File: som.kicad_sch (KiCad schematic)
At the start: 31 parts, among them J14 Conn_01x04, M1 jetson-orin-nx/nano-module, Q1 PJE138K, U4 NTS0102GT

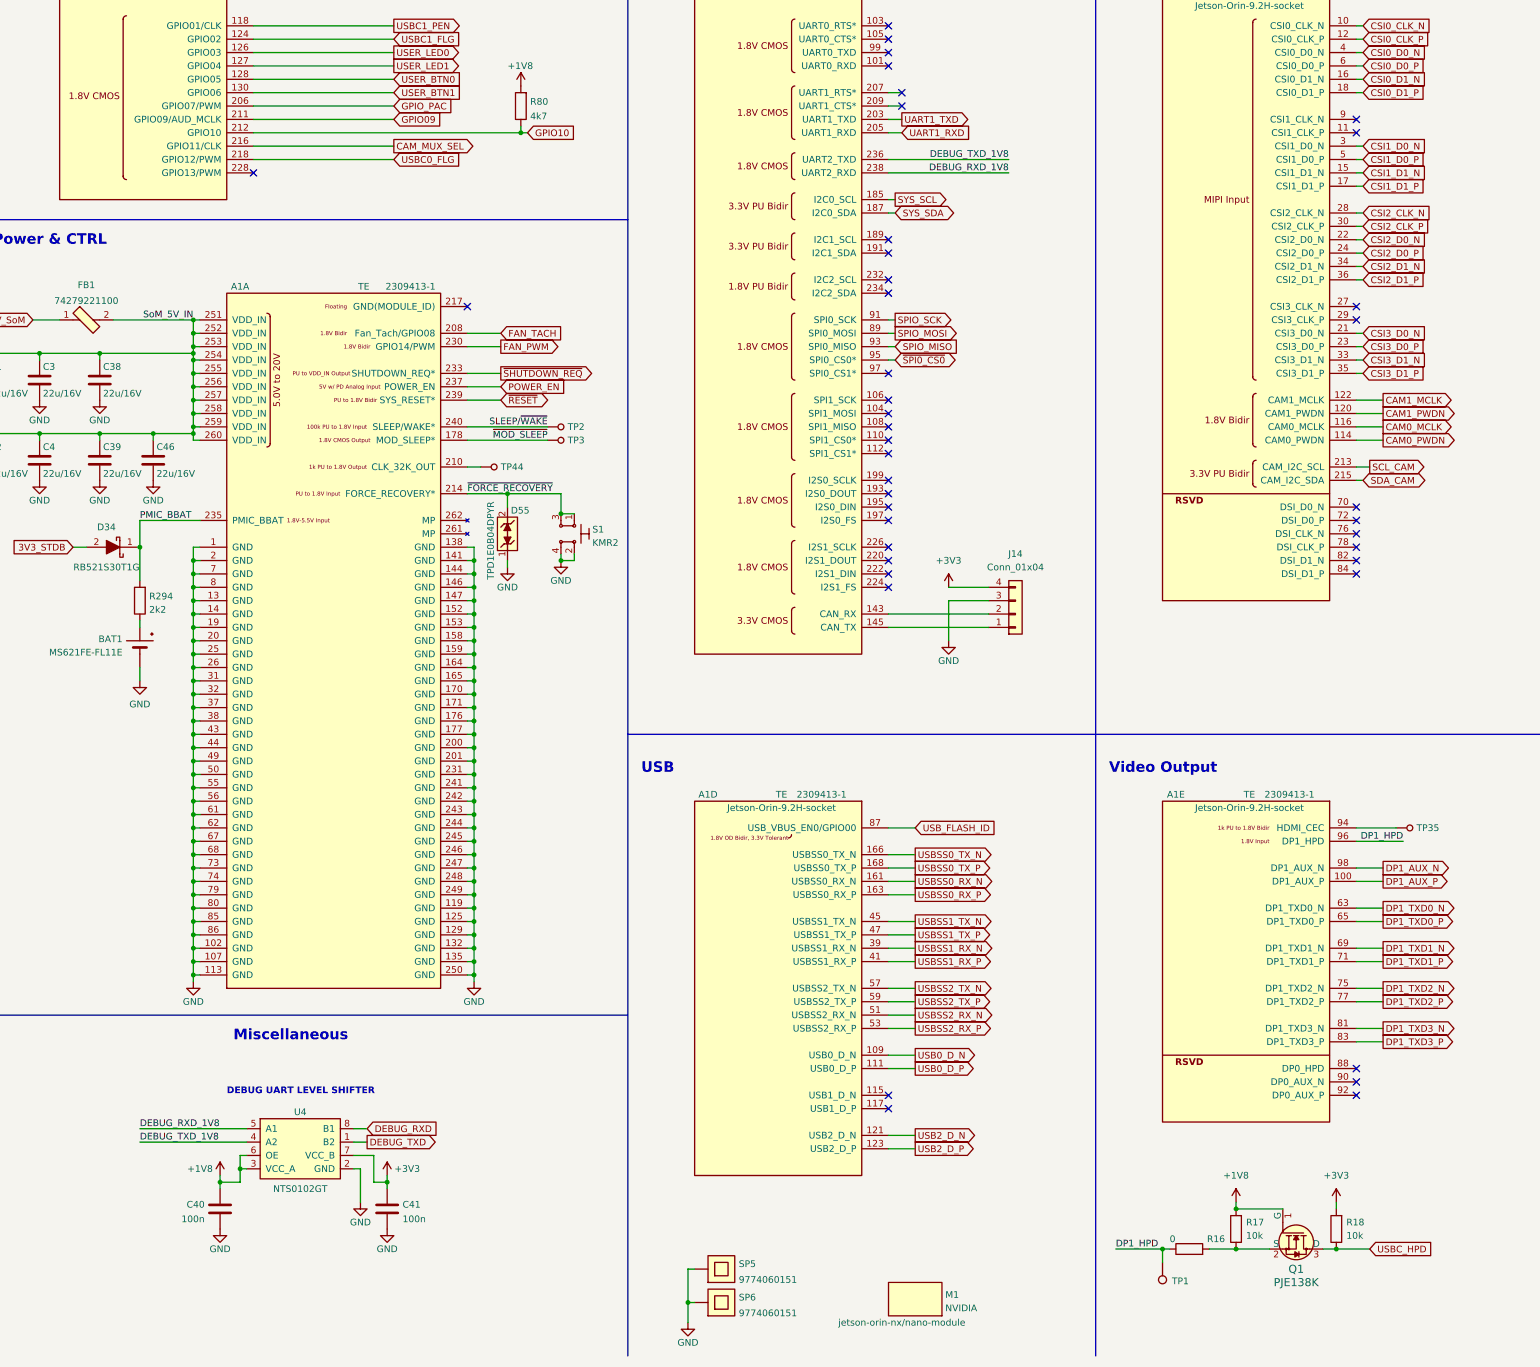
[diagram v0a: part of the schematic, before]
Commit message: Schematic V1 and footprints assigned
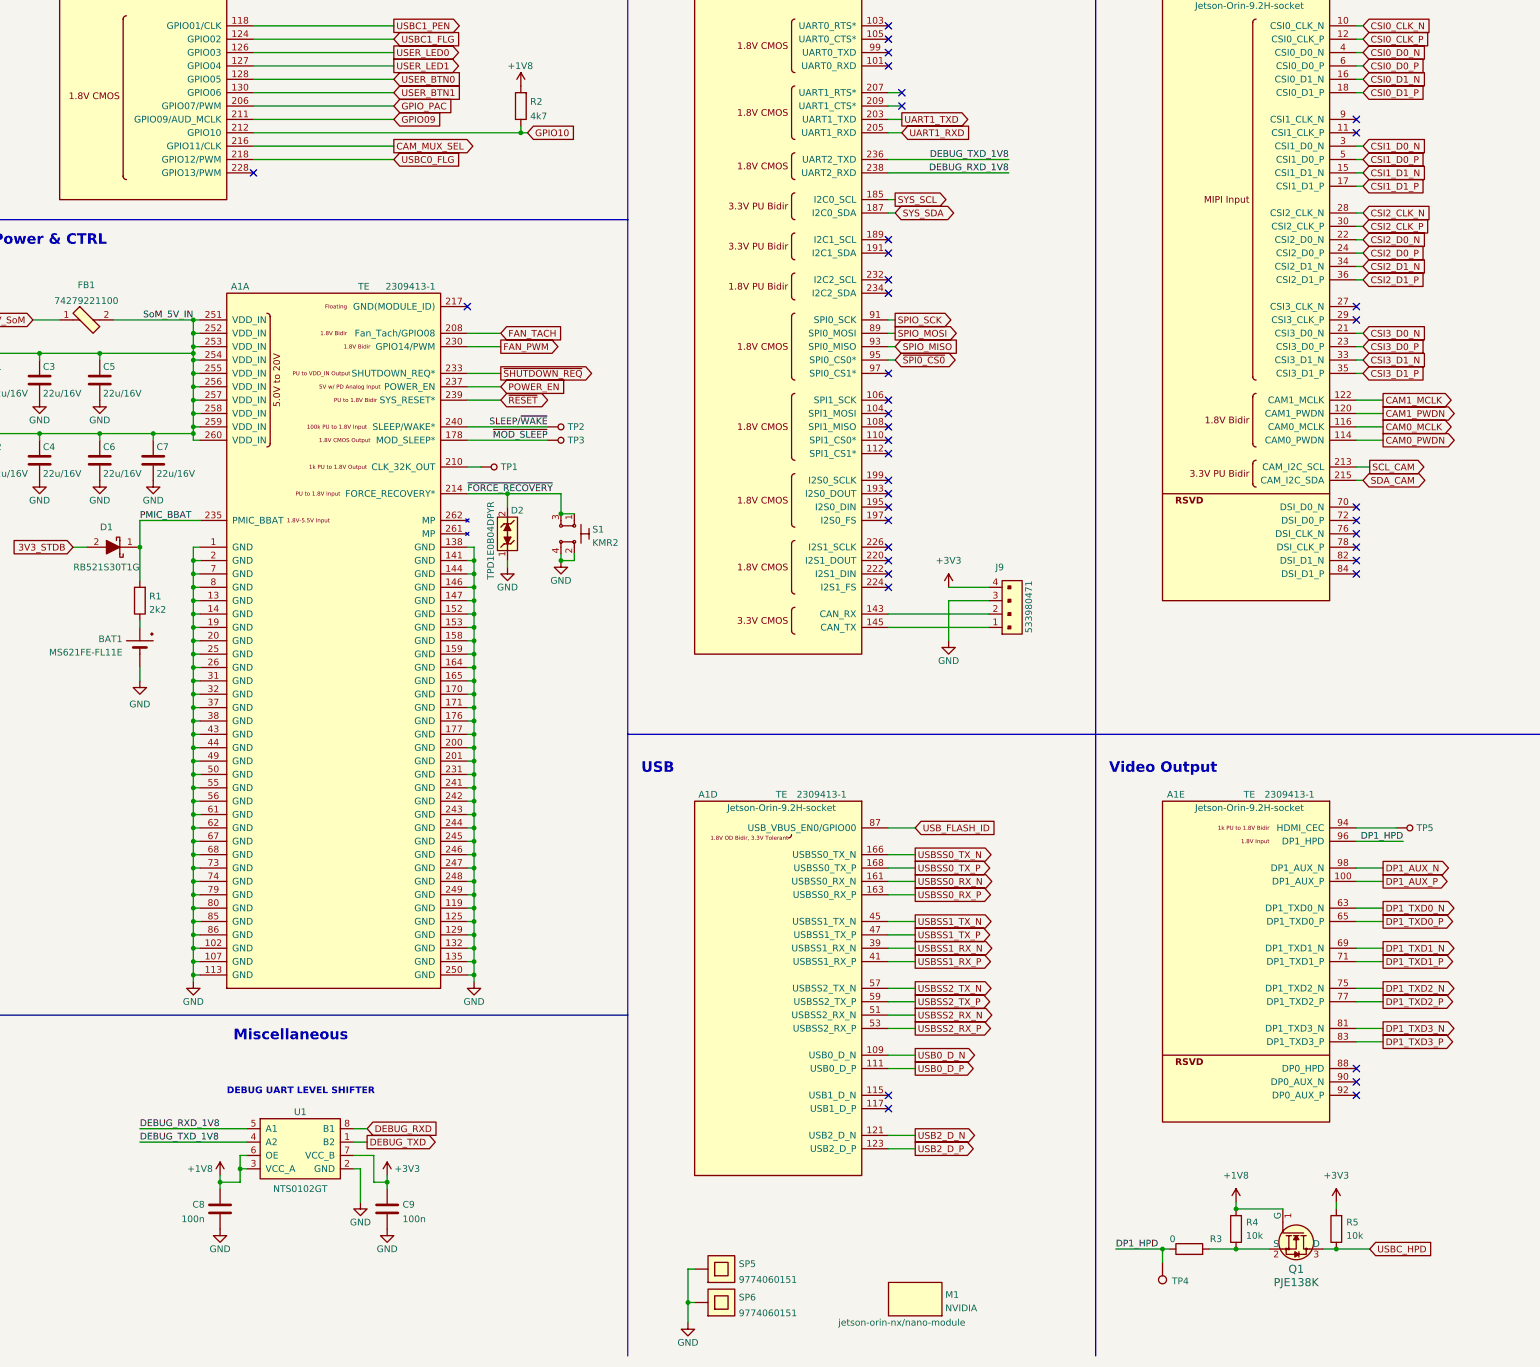
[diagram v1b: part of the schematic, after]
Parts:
- removed J14: Conn_01x04, symbol Connector_Generic:Conn_01x04
- added J9: 533980471, jetson-orin-baseboard-footprints:Molex_PicoBlade_53398-0471_1x04-1MP_P1.25mm_Vertical, symbol jetson-orin-baseboard:533980471
- R3: renamed from R16; footprint (none) -> jetson-orin-baseboard-footprints:0402-res
- R4: renamed from R17; footprint (none) -> jetson-orin-baseboard-footprints:0402-res
- R5: renamed from R18; footprint (none) -> jetson-orin-baseboard-footprints:0402-res
- TP4: renamed from TP1; footprint (none) -> jetson-orin-baseboard-footprints:Testpoint_smd_0_75mm
- renumbered C38 to C5, C39 to C6, C46 to C7, C40 to C8, C41 to C9, D34 to D1, D55 to D2, R294 to R1, R80 to R2, TP44 to TP1, TP35 to TP5, U4 to U1
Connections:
- net +3V3: now also J9.4
- net GND: now also J9.3
- net at A1.143 (CAN_RX): now also J9.2
- net at A1.145 (CAN_TX): now also J9.1

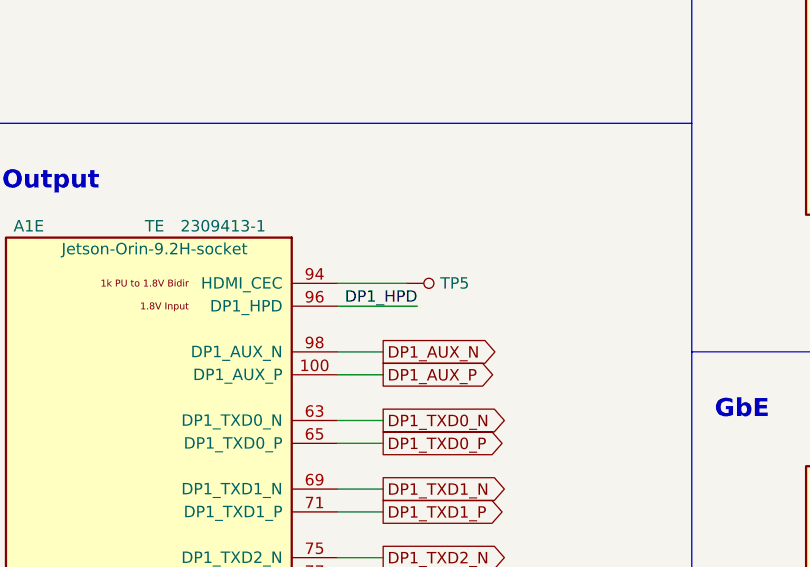
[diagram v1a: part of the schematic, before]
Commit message: Adding a no connect and removing a test point on hdmi_cec
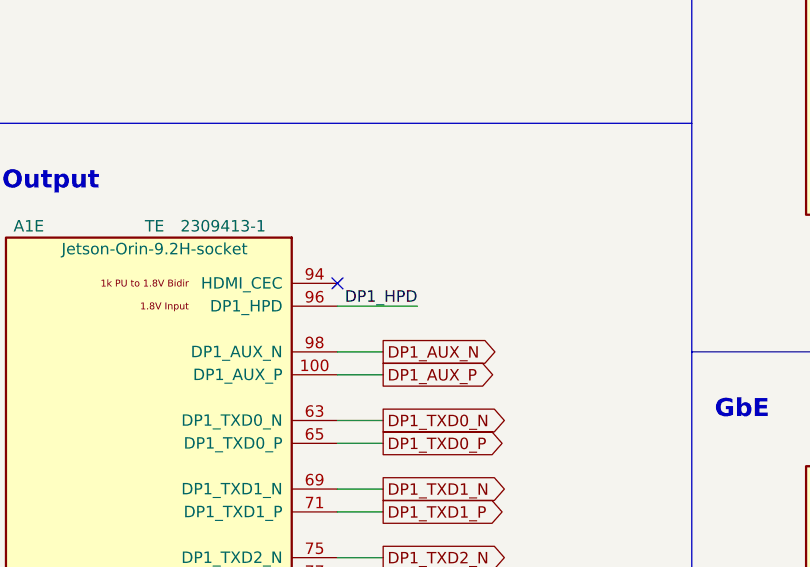
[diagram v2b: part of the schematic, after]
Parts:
- removed TP5: TP_SMD_0_75MM, jetson-orin-baseboard-footprints:Testpoint_smd_0_75mm, symbol jetson-orin-baseboard:TP_SMD_0_75MM
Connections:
- no-connect marks 65 -> 66
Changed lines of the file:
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@@
   (no_connect (at 367.03 116.84))
   (no_connect (at 367.03 142.24))
+  (no_connect (at 278.13 182.88))
   (no_connect (at 191.77 43.18))
   (no_connect (at 191.77 45.72))
@@
     (stroke (width 0) (type default))
   )
-  (wire (pts (xy 278.13 182.88) (xy 285.75 182.88))
-    (stroke (width 0) (type default))
-  )
   (wire (pts (xy 189.23 203.2) (xy 194.31 203.2))
     (stroke (width 0) (type default))
@@
     )
   )
-  (symbol (lib_id "jetson-orin-baseboard:TP_SMD_0_75MM") (at 288.29 182.88 90) (unit 1)
-    (in_bom yes) (on_board yes) (dnp no) (fields_autoplaced)
-    (property "Reference" "TP5" (at 289.56 182.8799 90)
-      (effects (font (size 1.27 1.27)) (justify right))
-    )
-    (property "Value" "TP_SMD_0_75MM" (at 290.83 182.88 0)
-      (effects (font (size 1.27 1.27)) hide)
-    )
-    (property "Footprint" "jetson-orin-baseboard-footprints:Testpoint_smd_0_75mm" (at 283.21 177.8 0)
-      (effects (font (size 1.524 1.524)) (justify left) hide)
-    )
-    (property "Datasheet" "" (at 280.67 177.8 0)
-      (effects (font (size 1.524 1.524)) (justify left) hide)
-    )
-    (pin "1")
-    (instances
-      (project "jetson-orin-baseboard"
-        (path "/4b393452-b11e-416e-bc83-918ae3cab2f1/68b67bb9-703f-4397-bb09-4d44d3a917ad"
-          (reference "TP5") (unit 1)
-        )
-      )
-    )
-  )
